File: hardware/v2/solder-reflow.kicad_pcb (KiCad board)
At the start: 2 copper layers, 86 x 65 mm, 91 parts, among them J1 ACCON, J10 PINOUT, J11 ST7789, J13 JTAG10, J2 OLED 0.91, J3 PTC_Con, J4 12V, J5 SSROUT2, J6 USB_B, J7 PINOUT, J8 PINOUT, J9 12VIN, K1 G3MB202PDC12, Q1 SS8550, Q2 SS8550, Q3 SS8050, Q4 SS8050, SW2 RST, SW3 IO0, SW4 D, SW5 U, SW6 L, SW7 R, U1 TL431LP, U2 TL074, U3 AMS1117-3.3, U4 L7805, U6 ESP32-WROOM-32D, U7 CH340C

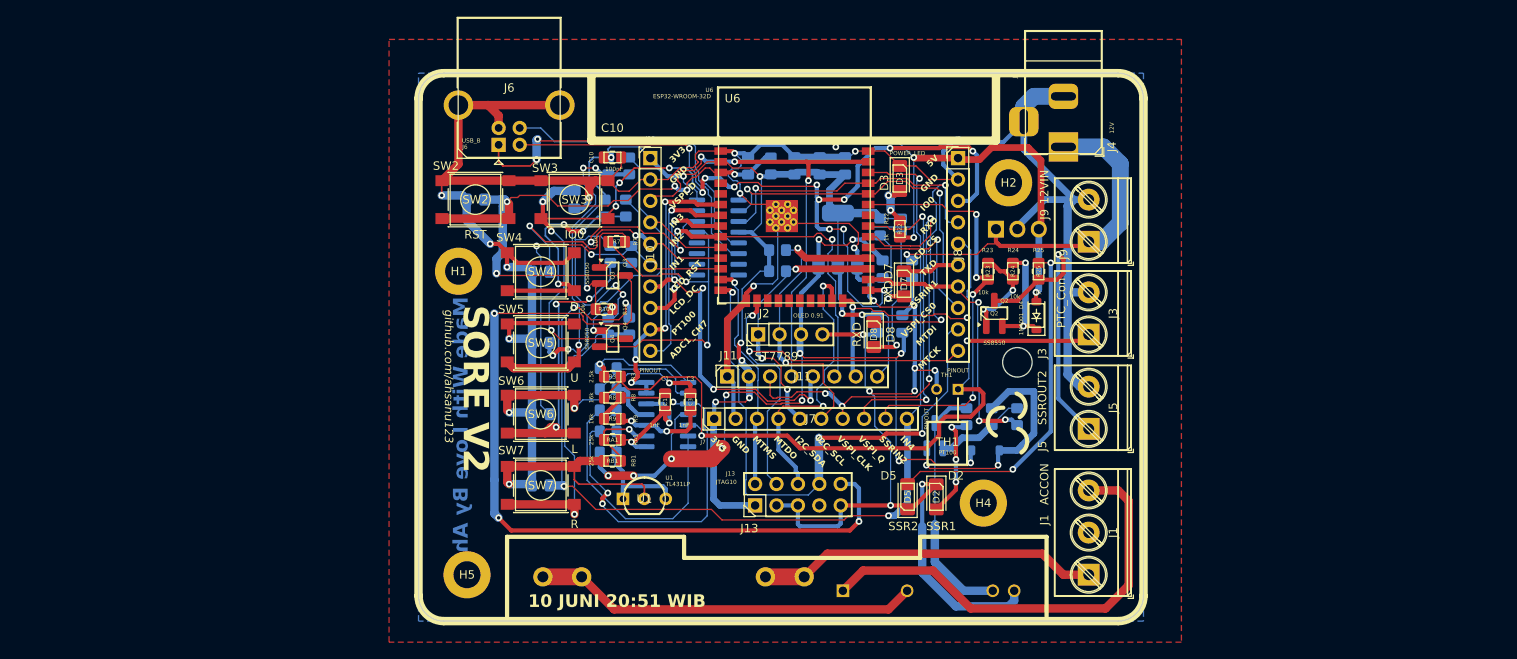
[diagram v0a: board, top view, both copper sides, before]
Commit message: feat: basic board layout finished
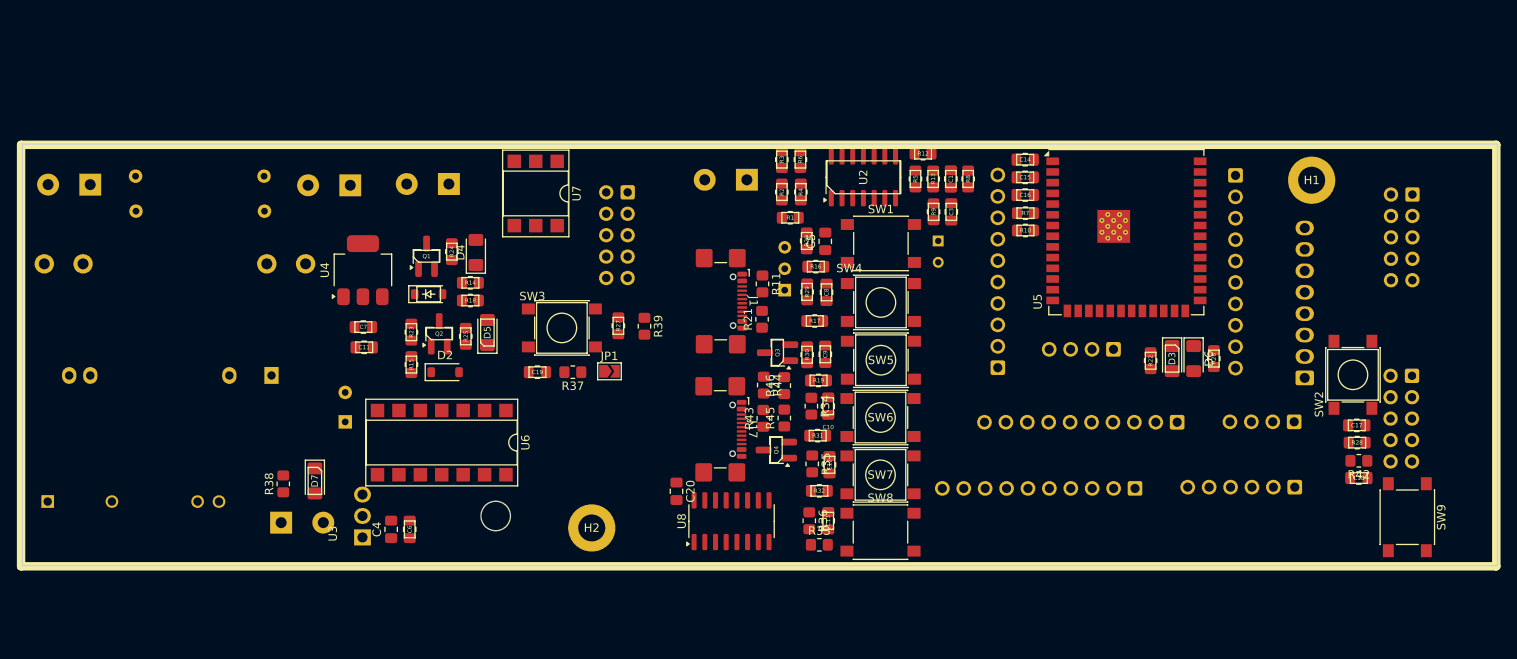
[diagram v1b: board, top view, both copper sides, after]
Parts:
- removed D8: RXD, LED_SMD:LED_1206_3216Metric_Pad1.42x1.75mm_HandSolder
- removed H4, H5: MountingHole_Pad, MountingHole:MountingHole_3.2mm_M3_DIN965_Pad
- removed J13: JTAG10, Connector_PinHeader_2.54mm:PinHeader_2x05_P2.54mm_Vertical
- removed RA1, RB1: 25k, Resistor_SMD:R_0805_2012Metric_Pad1.20x1.40mm_HandSolder
- added C20: 100nF, Capacitor_SMD:C_0805_2012Metric_Pad1.18x1.45mm_HandSolder, F.Cu at (133.1, 115.6)
- added C4: 0.33uF, Capacitor_SMD:C_0805_2012Metric_Pad1.18x1.45mm_HandSolder, F.Cu at (99.3, 120.1)
- added C5: 1uF, Capacitor_SMD:C_0805_2012Metric_Pad1.18x1.45mm_HandSolder, F.Cu at (150.7, 85.9)
- added D6: RXD, LED_SMD:LED_1206_3216Metric_Pad1.42x1.75mm_HandSolder, F.Cu at (194.4, 99.9)
- added J12: JTAG10, Connector_IDC:IDC-Header_2x05_P2.54mm_Vertical, B.Cu at (220.3, 101.9)
- added J14: SSROUT2, TerminalBlock_Phoenix:TerminalBlock_Phoenix_PT-1,5-2-5.0-H_1x02_P5.00mm_Horizontal, B.Cu at (106.1, 79.2)
- added J15: LCD_CONN, Connector_Molex:Molex_SL_171971-0010_1x10_P2.54mm_Vertical, B.Cu at (187.5, 115.3)
- added J16: UART, Connector_Molex:Molex_SL_171971-0004_1x04_P2.54mm_Vertical, B.Cu at (206.4, 107.4)
- added J17: USB_C_Receptacle_USB2.0_14P, Connector_USB:USB_C_Receptacle_GCT_USB4110, F.Cu at (137.2, 108.2)
- added J18: High_To_Low_Link, Connector_IDC:IDC-Header_2x05_P2.54mm_Vertical, B.Cu at (127.3, 80.1)
- added J19: High_To_Low_Link, Connector_IDC:IDC-Header_2x05_P2.54mm_Vertical, B.Cu at (220.4, 80.4)
- added JP1: InH11AA1, Jumper:SolderJumper-2_P1.3mm_Open_TrianglePad1.0x1.5mm, F.Cu at (125.2, 101.4)
- added PS1: HLK-2M12 12V 2W, Converter_ACDC:Converter_ACDC_Hi-Link_HLK-2Mxx, B.Cu at (85.1, 101.9)
- added R11: 5K1, Resistor_SMD:R_0805_2012Metric_Pad1.20x1.40mm_HandSolder, F.Cu at (143.3, 91.0)
- added R21: 5K1, Resistor_SMD:R_0805_2012Metric_Pad1.20x1.40mm_HandSolder, F.Cu at (143.2, 95.2)
- added R33: 10k, Resistor_SMD:R_0805_2012Metric_Pad1.20x1.40mm_HandSolder, F.Cu at (150.1, 122.0)
- added R34: 22k, Resistor_SMD:R_0805_2012Metric_Pad1.20x1.40mm_HandSolder, F.Cu at (149.1, 105.5)
- added R35: 22k, Resistor_SMD:R_0805_2012Metric_Pad1.20x1.40mm_HandSolder, F.Cu at (149.2, 112.3)
- added R36: 22k, Resistor_SMD:R_0805_2012Metric_Pad1.20x1.40mm_HandSolder, F.Cu at (148.9, 119.1)
- added R37: 22k, Resistor_SMD:R_0805_2012Metric_Pad1.20x1.40mm_HandSolder, F.Cu at (120.8, 101.5)
- added R38: 1k, Resistor_SMD:R_0805_2012Metric_Pad1.20x1.40mm_HandSolder, F.Cu at (86.5, 114.7)
- added R39: 10k, Resistor_SMD:R_0805_2012Metric_Pad1.20x1.40mm_HandSolder, F.Cu at (129.3, 96.0)
- added R40: 10k 1W, Resistor_THT:R_Axial_DIN0309_L9.0mm_D3.2mm_P15.24mm_Horizontal, B.Cu at (69.0, 82.4)
- added R41: 10k 1W, Resistor_THT:R_Axial_DIN0309_L9.0mm_D3.2mm_P15.24mm_Horizontal, B.Cu at (68.9, 78.2)
- added R42: 1k, Resistor_SMD:R_0805_2012Metric_Pad1.20x1.40mm_HandSolder, F.Cu at (214.0, 112.0)
- added R43: 5K1, Resistor_SMD:R_0805_2012Metric_Pad1.20x1.40mm_HandSolder, F.Cu at (143.4, 107.0)
- added R44: 5K1, Resistor_SMD:R_0805_2012Metric_Pad1.20x1.40mm_HandSolder, F.Cu at (143.4, 103.0)
- added R45: 10k, Resistor_SMD:R_0805_2012Metric_Pad1.20x1.40mm_HandSolder, F.Cu at (145.9, 106.9)
- added R46: 10k, Resistor_SMD:R_0805_2012Metric_Pad1.20x1.40mm_HandSolder, F.Cu at (145.9, 103.1)
- added SW1: L, Button_Switch_SMD:SW_Push_1P1T_NO_6x6mm_H9.5mm, F.Cu at (157.4, 86.2)
- added SW8: R, Button_Switch_SMD:SW_Push_1P1T_NO_6x6mm_H9.5mm, F.Cu at (157.3, 120.5)
- added SW9: Boot, Button_Switch_SMD:SW_Push_1P1T_NO_6x6mm_H9.5mm, F.Cu at (219.8, 118.7)
- added U5: ESP32-S3-WROOM-1, RF_Module:ESP32-S3-WROOM-1U, F.Cu at (186.5, 84.9)
- added U8: CH340C, Package_SO:SOIC-16_3.9x9.9mm_P1.27mm, F.Cu at (139.6, 119.2)
- C1, C3: value 1nF -> 10nF
- C10: value 100nF -> 1uF
- C11, C15: value 100nF -> 22uF; moved to F.Cu
- C12: value 100nF -> 1uF; moved to F.Cu
- C13, C8, C9: value 22uF -> 1uF; moved to F.Cu
- C14, C16, C19, D1, Q1, R1, R14, R15, R16, R17, R19, R2, R26, R28, R29, R30, R4, R5, R6: moved to F.Cu
- C17, C18: value 1uF -> 100nF; moved to F.Cu
- C2: value 1uF -> 100uF/16V; footprint Capacitor_SMD:C_0805_2012Metric_Pad1.18x1.45mm_HandSolder -> Capacitor_THT:CP_Radial_D8.0mm_P3.50mm
- C6: value 0.33uF -> 0.1uF; moved to F.Cu
- C7: value 0.1uF -> 22uF; moved to F.Cu
- D2: value SSR1 -> 1N4001; footprint LED_SMD:LED_1206_3216Metric_Pad1.42x1.75mm_HandSolder -> Diode_SMD:D_SOD-123
- D3: value POWER_LED -> TXD
- D4: value 1N4001 -> SSR2; footprint Diode_SMD:D_SOD-123 -> LED_SMD:LED_1206_3216Metric_Pad1.42x1.75mm_HandSolder
- D5: value SSR2 -> SSR1
- D7: value TXD -> POWER_LED
- J1: value ACCON -> USB_C_Receptacle_USB2.0_14P; footprint TerminalBlock_Phoenix:TerminalBlock_Phoenix_PT-1,5-3-5.0-H_1x03_P5.00mm_Horizontal -> Connector_USB:USB_C_Receptacle_GCT_USB4110
- J10, J7, J8: footprint Connector_PinHeader_2.54mm:PinHeader_1x10_P2.54mm_Vertical -> Connector_Molex:Molex_SL_171971-0010_1x10_P2.54mm_Vertical; moved to B.Cu
- J11: value ST7789 -> I2C; footprint Connector_PinSocket_2.54mm:PinSocket_1x08_P2.54mm_Vertical -> Connector_Molex:Molex_SL_171971-0004_1x04_P2.54mm_Vertical; moved to B.Cu
- J2: value OLED 0.91 -> I2S; footprint Connector_PinHeader_2.54mm:PinHeader_1x04_P2.54mm_Vertical -> Connector_Molex:Molex_SL_171971-0006_1x06_P2.54mm_Vertical; moved to B.Cu
- J3, J9, TH1, U1: moved to B.Cu
- J4: value 12V -> 220V; footprint Connector_BarrelJack:BarrelJack_Horizontal -> TerminalBlock_Phoenix:TerminalBlock_Phoenix_PT-1,5-2-5.0-H_1x02_P5.00mm_Horizontal; moved to B.Cu
- J5: value SSROUT2 -> HEATER; moved to B.Cu
- J6: value USB_B -> InputButton; footprint Connector_USB:USB_B_OST_USB-B1HSxx_Horizontal -> Connector_Molex:Molex_KK-254_AE-6410-08A_1x08_P2.54mm_Vertical; moved to B.Cu
- R10, R7: value 10k -> 4K7
- R12: value 4K7 -> 9K1; moved to F.Cu
- R13: value 4K7 -> 1K; moved to F.Cu
- R18, R27: value 1k -> 10k; moved to F.Cu
- R20: value 10k -> 22k; moved to F.Cu
- R24: value 10k -> 1k
- R31, R32: value 22k -> 10k; moved to F.Cu
- SW3: value IO0 -> SWH11AA1
- SW6: value L -> R
- U2: value TL074 -> LM324; moved to F.Cu
- U3: value AMS1117-3.3 -> L7805; footprint Package_TO_SOT_SMD:SOT-223-3_TabPin2 -> Package_TO_SOT_THT:TO-220F-3_Horizontal_TabDown
- U4: value L7805 -> AMS1117-3.3; footprint Package_TO_SOT_THT:TO-220F-3_Horizontal_TabDown -> Package_TO_SOT_SMD:SOT-223-3_TabPin2; moved to F.Cu
- U6: value ESP32-WROOM-32D -> 74LS14; footprint RF_Module:ESP32-WROOM-32D -> Package_DIP:DIP-14_W7.62mm_SMDSocket_SmallPads
- U7: value CH340C -> H11AA1; footprint Package_SO:SOIC-16_3.9x9.9mm_P1.27mm -> Package_DIP:DIP-6_W7.62mm_SMDSocket_SmallPads; moved to F.Cu
- moved J4 115.5 mm to (63.6, 79.2), turned to 180 degrees
- moved SW2 106.2 mm to (213.3, 101.8), turned to 90 degrees
- moved H1 101.8 mm to (208.4, 78.7)
- moved J9 101.4 mm to (86.2, 119.3), turned to 0 degrees
- moved J6 99.5 mm to (207.6, 102.2)
- moved C18 97.3 mm to (214.0, 114.0), turned to 0 degrees
- moved C17 97.3 mm to (213.8, 107.8)
- moved K1 94.9 mm to (68.7, 115.4)
- moved J5 92.2 mm to (94.4, 79.3), turned to 180 degrees
- moved R28 76.9 mm to (213.8, 109.8), turned to 0 degrees
- moved U4 75.3 mm to (95.9, 89.4), turned to 90 degrees
- moved D7 73.7 mm to (90.2, 114.4)
- moved R15 72.1 mm to (101.7, 100.6), turned to -90 degrees
- moved F1 69.8 mm to (89.1, 88.6)
- moved R23 68.8 mm to (101.7, 96.7), turned to -90 degrees
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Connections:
- C1 pad 1: Net-(U2D-+) -> Net-(U2C--)
- C10 pad 1: +3.3V -> /IN4
- C11 pad 1: /EN -> +3.3V
- C12 pad 1: +3.3V -> /IN5
- C13 pad 1: +3.3V -> /IN6
- C14 pad 1: /EN -> +3.3V
- C15 pad 1: /IO0 -> +3.3V
- C16 pad 1: /IN2 -> +3.3V
- C17 pad 1: /IN3 -> /EN
- C18 pad 1: /IN1 -> /IO0
- C19 pad 1: /IN4 -> Net-(JP1-A)
- C2 pad 1: +3.3V -> +12V
- C6 pad 1: +12V -> +5V
- C8 pad 1: +5V -> /IN2
- C9 pad 1: +3.3V -> /IN3
- D2 pad 1: GND -> Net-(D2-K)
- D2 pad 2: Net-(D2-A) -> +5V
- D3 pad 1: GND -> /TXD0
- D4 pad 1: Net-(D4-K) -> GND
- D4 pad 2: +5V -> Net-(D4-A)
- D7 pad 1: /TXD -> GND
- F1 pad 1: AC -> LINE
- F1 pad 2: Net-(K1-L2) -> Net-(J4-Pin_1)
- J10 pad 1: +3.3V -> /SSRIN1
- J10 pad 10: /ADC1_CH7 -> /CS0
- J10 pad 2: GND -> /SSRIN2
- J10 pad 3: /VSPI_D -> /ZC_INPUT
- J10 pad 4: /IN3 -> /PT100
- J10 pad 5: /IN2 -> /IO5
- J10 pad 6: /IN1 -> /I2C_SDA
- J10 pad 7: /LCD_RST -> /I2C_SCL
- J10 pad 8: /LCD_DC -> /IO8
- J10 pad 9: /PT100 -> /QUADHD
- J11 pad 1: GND -> +3.3V
- J11 pad 2: +3.3V -> /I2C_SDA
- J11 pad 3: /VSPI_CLK -> /I2C_SCL
- J11 pad 4: /VSPI_D -> GND
- J2 pad 1: /I2C_SDA -> +3.3V
- J2 pad 2: /I2C_SCL -> /MCLK
- J2 pad 3: +5V -> /BCLK
- J2 pad 4: GND -> /WS
- J4 pad 1: +12V -> Net-(J4-Pin_1)
- J4 pad 2: GND -> NEUT
- J5 pad 1: Net-(J5-Pin_1) -> LINE
- J5 pad 2: GND -> Net-(J5-Pin_2)
- J6 pad 1: +5V -> /sw1
- J6 pad 2: Net-(J6-D-) -> /sw2
- J6 pad 3: Net-(J6-D+) -> /sw3
- J6 pad 4: GND -> /sw4
- J6 pad 5: GND -> /sw5
- J7 pad 1: +3.3V -> /MOSI
- J7 pad 10: /IN4 -> /IN5
- J7 pad 2: GND -> /SCLK
- J7 pad 3: /MTMS -> /MISO
- J7 pad 4: /MTDO -> /QUADWP
- J7 pad 5: /I2C_SDA -> /IN1
- J7 pad 6: /I2C_SCL -> /IN2
- J7 pad 7: /VSPI_CLK -> /TXD0
- J7 pad 8: /VSPI_Q -> /RXD0
- J7 pad 9: /SSRIN2 -> /IN4
- J8 pad 1: +5V -> /IN6
- J8 pad 10: /MTCK -> /DIO
- J8 pad 2: GND -> /MCLK
- J8 pad 3: /IO0 -> /MTCK
- J8 pad 4: /RXD -> /MTDO
- J8 pad 5: /LCD_CS -> /MTDI
- J8 pad 6: /TXD -> /MTMS
- J8 pad 7: /SSRIN1 -> /BCLK
- J8 pad 8: /VSPI_CS0 -> /IN3
- J8 pad 9: /MTDI -> /WS
- K1 pad 1: Net-(J1-Pin_3) -> Net-(J5-Pin_2)
- K1 pad 2: Net-(K1-L2) -> NEUT
- Q1 pad 3: Net-(K1-+) -> Net-(J14-Pin_1)
- Q2 pad 2: Net-(D4-K) -> Net-(D2-K)
- Q2 pad 3: Net-(J5-Pin_1) -> Net-(K1-+)
- R10 pad 1: Net-(Q4-B) -> /I2C_SCL
- R10 pad 2: /RTS -> +3.3V
- R12 pad 1: /I2C_SDA -> /PT100
- R12 pad 2: +3.3V -> Net-(U2D--)
- R13 pad 1: /I2C_SCL -> Net-(U2D--)
- R13 pad 2: +3.3V -> GND
- R15 pad 1: /SSRIN1 -> Net-(Q2-B)
- R15 pad 2: Net-(Q1-B) -> Net-(D2-K)
- R16 pad 2: Net-(R16-Pad2) -> /sw1
- R17 pad 2: Net-(R17-Pad2) -> /sw2
- R18 pad 1: Net-(D2-A) -> /SSRIN2
- R18 pad 2: Net-(K1-+) -> Net-(Q1-B)
- R19 pad 2: Net-(R19-Pad2) -> /sw3
- R20 pad 1: +3.3V -> /IN1
- R20 pad 2: Net-(R20-Pad2) -> /sw1
- R22 pad 1: Net-(D3-A) -> +3.3V
- R22 pad 2: +5V -> Net-(D3-A)
- R23 pad 1: /SSRIN2 -> /SSRIN1
- R24 pad 1: Net-(Q2-B) -> Net-(D4-A)
- R24 pad 2: Net-(D4-K) -> Net-(J14-Pin_1)
- R25 pad 2: Net-(J5-Pin_1) -> Net-(K1-+)
- R26 pad 2: Net-(D7-A) -> Net-(D6-A)
- R27 pad 2: Net-(D8-A) -> Net-(R27-Pad2)
- R29 pad 1: /IN1 -> /IN2
- R29 pad 2: Net-(R16-Pad2) -> /sw2
- R30 pad 1: /IN2 -> /IN3
- R30 pad 2: Net-(R17-Pad2) -> /sw3
- R31 pad 1: /IN3 -> +3.3V
- R31 pad 2: Net-(R19-Pad2) -> /sw4
- R32 pad 1: /IN4 -> +3.3V
- R32 pad 2: Net-(R20-Pad2) -> /sw5
- R7 pad 1: Net-(Q3-B) -> /I2C_SDA
- R7 pad 2: /DTR -> +3.3V
- SW3 pad 2: /IO0 -> Net-(R27-Pad2)
- SW4 pad 2: Net-(R17-Pad2) -> /sw2
- SW5 pad 2: Net-(R19-Pad2) -> /sw3
- SW6 pad 2: Net-(R16-Pad2) -> /sw4
- SW7 pad 2: Net-(R20-Pad2) -> /sw5
- U2 pad 12: Net-(U2D-+) -> Net-(U2C--)
- U2 pad 13: /PT100 -> Net-(U2D--)
- U2 pad 8: Net-(U2D-+) -> Net-(U2C--)
- U3 pad 1: GND -> +12V
- U3 pad 2: +3.3V -> GND
- U4 pad 1: +12V -> GND
- U4 pad 2: GND -> +3.3V
- U6 pad 1: GND -> Net-(R39-Pad2)
- U6 pad 10: /IN3 -> (no net)
- U6 pad 11: /IN2 -> (no net)
- U6 pad 12: /IN1 -> (no net)
- U6 pad 13: /MTMS -> (no net)
- U6 pad 14: /MTDI -> +5V
- U6 pad 2: +3.3V -> /ZC_INPUT
- U6 pad 3: /EN -> (no net)
- U6 pad 4: unconnected-(U6-SENSOR_VP-Pad4) -> (no net)
- U6 pad 5: unconnected-(U6-SENSOR_VN-Pad5) -> (no net)
- U6 pad 6: /PT100 -> (no net)
- U6 pad 7: /ADC1_CH7 -> GND
- U6 pad 8: /LCD_RST -> (no net)
- U6 pad 9: /LCD_DC -> (no net)
- U7 pad 1: GND -> Net-(R40-Pad2)
- U7 pad 2: /TXD -> Net-(R41-Pad2)
- U7 pad 3: /RXD -> unconnected-(U7-NC-Pad3)
- U7 pad 4: +3.3V -> GND
- U7 pad 5: Net-(J6-D+) -> Net-(R39-Pad2)
- U7 pad 6: Net-(J6-D-) -> Net-(JP1-B)
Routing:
- net GND: track 482.1 -> 0.00 mm, vias 23 -> 0
- net +5V: track 222.0 -> 0.00 mm, vias 18 -> 0
- net /EN: track 173.1 -> 0.00 mm, vias 8 -> 0
- net +3.3V: track 169.2 -> 0.00 mm, vias 11 -> 0
- net /IO0: track 126.8 -> 0.00 mm, vias 17 -> 0
- net /IN4: track 123.0 -> 0.00 mm, vias 5 -> 0
- net /PT100Voltage: track 86.2 -> 0.00 mm, vias 2 -> 0
- net /VSPI_D: track 72.5 -> 0.00 mm, vias 3 -> 0
- net /MTDI: track 68.0 -> 0.00 mm, vias 3 -> 0
- net /RXD: track 60.8 -> 0.00 mm, vias 3 -> 0
- net /VSPI_CLK: track 55.2 -> 0.00 mm, vias 4 -> 0
- net Net-(J1-Pin_3): track 53.2 -> 0.00 mm
- net /MTCK: track 52.0 -> 0.00 mm, vias 2 -> 0
- net /SSRIN2: track 49.1 -> 0.00 mm, vias 4 -> 0
- net /LCD_RST: track 48.8 -> 0.00 mm, vias 5 -> 0
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- removed copper zone on F.Cu, net (none)
- removed copper zone on B.Cu, net GND
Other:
- board size 86 x 65 mm -> 175 x 50 mm
- board text added: "HIGH"
- board text added: "LOW"
- board text removed: "10 JUNI 20:51 WIB"
- board text removed: "3V3"
- board text removed: "5V"
- board text removed: "ADC1_CH7"
- board text removed: "GND"
- board text removed: "I2C_SCL"
- board text removed: "I2C_SDA"
- board text removed: "IN1"
- board text removed: "IN2"
- board text removed: "IN3"
- board text removed: "IN4"
- board text removed: "IO0"
- board text removed: "LCD_CS"
- board text removed: "LCD_DC"
- board text removed: "LCD_RST"
- board text removed: "MTCK"
- board text removed: "MTDI"
- board text removed: "MTDO"
- board text removed: "MTMS"
- board text removed: "Made With Love By Ah"
- board text removed: "PT100"
- board text removed: "RXD"
- board text removed: "SORE Solder Reflow"
- board text removed: "SORE V2"
- board text removed: "SSRIN1"
- board text removed: "SSRIN2"
- board text removed: "TXD"
- board text removed: "VSPI_CLK"
- board text removed: "VSPI_CS0"
- board text removed: "VSPI_D"
- board text removed: "VSPI_Q"
- board text removed: "github.com/ahsanu123"

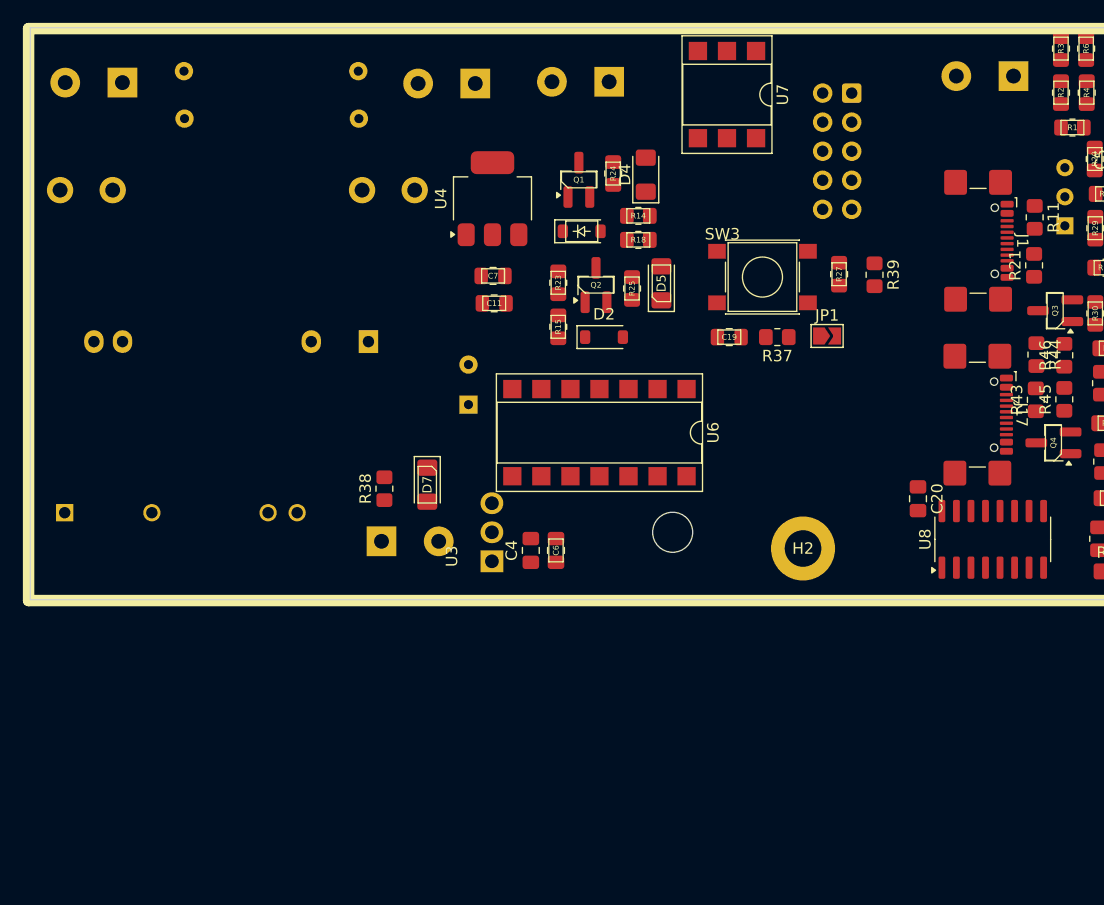
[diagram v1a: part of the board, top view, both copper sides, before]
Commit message: feat: routing part 1
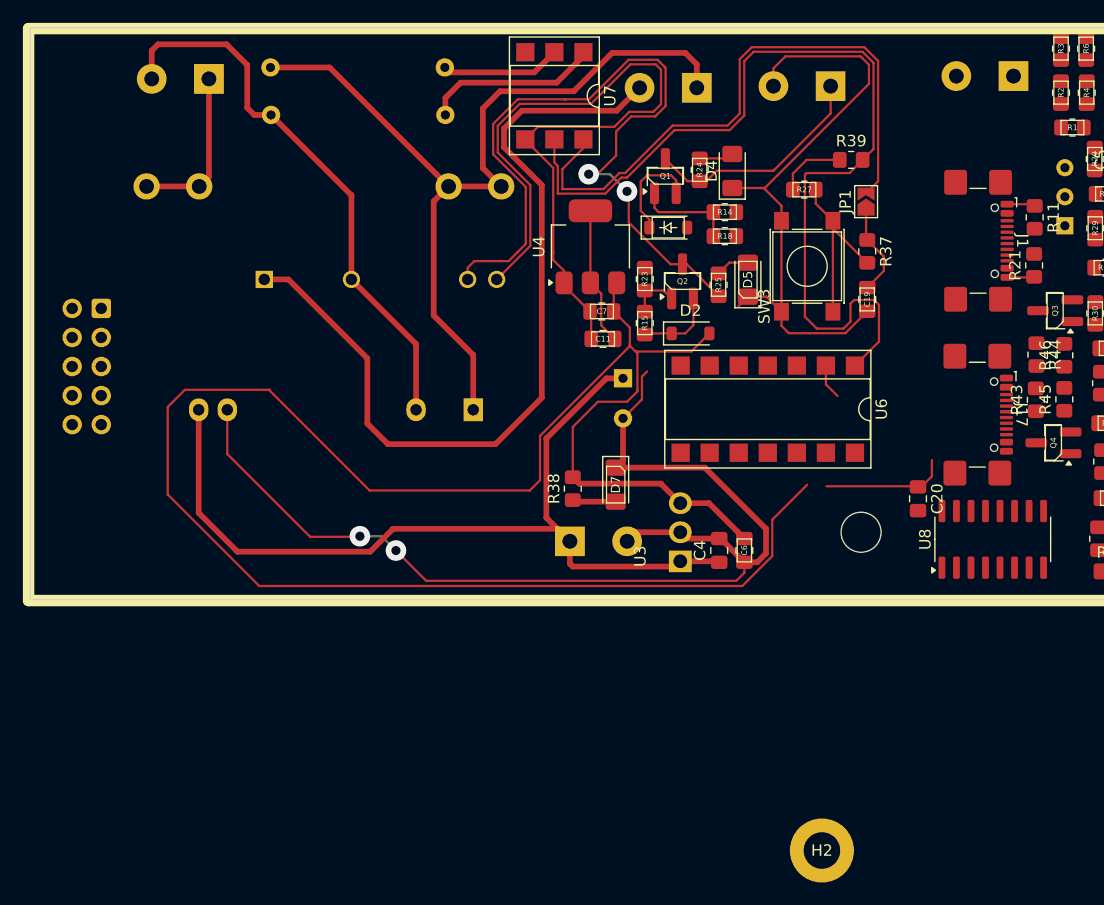
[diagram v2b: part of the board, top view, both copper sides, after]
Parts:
- moved J18 68.3 mm to (61.7, 99.0)
- moved K1 26.8 mm to (86.1, 95.0)
- moved H2 26.5 mm to (124.7, 146.3)
- moved J14 19.4 mm to (125.5, 79.5)
- moved J5 19.4 mm to (113.8, 79.7)
- moved U3 16.5 mm to (112.3, 121.1)
- moved C4 16.5 mm to (115.7, 120.1)
- moved C6 16.5 mm to (117.9, 120.1)
- moved D7 16.5 mm to (106.7, 114.4)
- moved J9 16.5 mm to (102.7, 119.3)
- moved R38 16.5 mm to (102.9, 114.7)
- moved U7 15.1 mm to (101.3, 80.4)
- moved U6 14.9 mm to (120.0, 107.8)
- moved C2 13.7 mm to (107.3, 105.1), turned to -90 degrees
- moved C19 12.5 mm to (128.7, 98.2), turned to -90 degrees
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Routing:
- net GND: track 0.00 -> 223.4 mm, vias 0 -> 2
- net +5V: track 0.00 -> 171.4 mm
- net Net-(R39-Pad2): track 0.00 -> 82.9 mm
- net +12V: track 0.00 -> 78.2 mm
- net LINE: track 0.00 -> 76.6 mm
- net Net-(J5-Pin_2): track 0.00 -> 73.5 mm
- net Net-(K1-+): track 0.00 -> 67.7 mm, vias 0 -> 2
- net Net-(JP1-B): track 0.00 -> 53.1 mm
- net NEUT: track 0.00 -> 48.9 mm
- net +3.3V: track 0.00 -> 29.1 mm
- net Net-(J14-Pin_1): track 0.00 -> 20.1 mm
- net Net-(R27-Pad2): track 0.00 -> 16.2 mm
- net Net-(R40-Pad2): track 0.00 -> 15.4 mm
- net Net-(J4-Pin_1): track 0.00 -> 14.4 mm
- net Net-(R41-Pad2): track 0.00 -> 10.5 mm
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
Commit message: feat: routing part 2
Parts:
- moved R22 29.6 mm to (206.7, 76.2), turned to 0 degrees
- moved J6 29.2 mm to (178.4, 100.2), turned to -90 degrees
- moved D3 25.8 mm to (206.1, 78.4), turned to 0 degrees
- moved R42 22.9 mm to (205.8, 90.5), turned to 0 degrees
- moved C18 22.9 mm to (205.8, 92.6), turned to 180 degrees
- moved R28 22.8 mm to (205.8, 88.5)
- moved C17 22.8 mm to (205.8, 86.5)
- moved J10 22.8 mm to (169.8, 78.2), turned to -90 degrees
- moved SW9 22.5 mm to (212.3, 97.5)
- moved D6 22.1 mm to (206.1, 81.0), turned to 0 degrees
- moved R26 19.3 mm to (206.7, 83.2), turned to 0 degrees
- moved J11 17.3 mm to (169.8, 107.2), turned to -90 degrees
- moved J7 15.2 mm to (186.6, 121.3), turned to 90 degrees
- moved SW2 15.0 mm to (212.2, 86.9), turned to -90 degrees
- moved R4 14.1 mm to (159.7, 87.8), turned to 0 degrees
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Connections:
- J10 pad 1: /SSRIN1 -> /PT100
- J10 pad 10: /CS0 -> /USB_D-
- J10 pad 2: /SSRIN2 -> /IO5
- J10 pad 3: /ZC_INPUT -> /I2C_SDA
- J10 pad 4: /PT100 -> /I2C_SCL
- J10 pad 5: /IO5 -> /IN1
- J10 pad 6: /I2C_SDA -> /IN2
- J10 pad 7: /I2C_SCL -> /IN4
- J10 pad 8: /IO8 -> /IN5
- J10 pad 9: /QUADHD -> /IO8
- J7 pad 1: /MOSI -> /USB_D+
- J7 pad 10: /IN5 -> /IN6
- J7 pad 2: /SCLK -> /ZC_INPUT
- J7 pad 3: /MISO -> /IN3
- J7 pad 4: /QUADWP -> /QUADHD
- J7 pad 5: /IN1 -> /CS0
- J7 pad 6: /IN2 -> /MOSI
- J7 pad 7: /TXD0 -> /SCLK
- J7 pad 8: /RXD0 -> /MISO
- J7 pad 9: /IN4 -> /QUADWP
- J8 pad 1: /IN6 -> /TXD0
- J8 pad 10: /DIO -> /WS
- J8 pad 2: /MCLK -> /RXD0
- J8 pad 3: /MTCK -> /MTMS
- J8 pad 4: /MTDO -> /MTDI
- J8 pad 5: /MTDI -> /MTDO
- J8 pad 6: /MTMS -> /MTCK
- J8 pad 7: /BCLK -> /MCLK
- J8 pad 8: /IN3 -> /BCLK
- J8 pad 9: /WS -> /DIO
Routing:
- net GND: track 223.4 -> 467.1 mm
- net +3.3V: track 29.1 -> 86.1 mm
- net /sw6: track 0.00 -> 41.4 mm
- net /PT100: track 0.00 -> 38.9 mm
- net /USB_D+: track 0.00 -> 37.5 mm
- net +5V: track 171.4 -> 208.1 mm
- net /ZC_INPUT: track 3.08 -> 33.6 mm
- net /IN3: track 0.00 -> 29.6 mm
- net /IO0: track 0.00 -> 26.8 mm
- net /QUADHD: track 0.00 -> 24.3 mm
- net /CS0: track 0.00 -> 21.7 mm
- net /PT100Voltage: track 0.00 -> 20.9 mm
- net Net-(U2A-+): track 0.00 -> 20.5 mm
- net /MOSI: track 0.00 -> 19.0 mm
- net /USB_D-: track 0.00 -> 17.4 mm
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
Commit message: feat: attempt to finish routing
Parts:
- removed J10: PINOUT, Connector_Molex:Molex_SL_171971-0010_1x10_P2.54mm_Vertical
- removed J12: JTAG10, Connector_IDC:IDC-Header_2x05_P2.54mm_Vertical
- removed J18, J19: High_To_Low_Link, Connector_IDC:IDC-Header_2x05_P2.54mm_Vertical
- removed R12: 9K1, Resistor_SMD:R_0805_2012Metric_Pad1.20x1.40mm_HandSolder
- removed R13: 1K, Resistor_SMD:R_0805_2012Metric_Pad1.20x1.40mm_HandSolder
- removed R2, R4, R5, R6: 25k, Resistor_SMD:R_0805_2012Metric_Pad1.20x1.40mm_HandSolder
- removed R3: 2.5k, Resistor_SMD:R_0805_2012Metric_Pad1.20x1.40mm_HandSolder
- removed R8, R9: 16k, Resistor_SMD:R_0805_2012Metric_Pad1.20x1.40mm_HandSolder
- removed TH1: PT100, Package_TO_SOT_THT:TO-92-2_Horizontal2
- removed U1: TL431LP, Package_TO_SOT_THT:TO-92_Inline_Wide
- removed U2: LM324, Package_SO:SOIC-14_3.9x8.7mm_P1.27mm
- added C21: 100nF, Capacitor_SMD:C_0805_2012Metric_Pad1.18x1.45mm_HandSolder, F.Cu at (173.3, 99.8)
- added J13: RTD_PT100, TerminalBlock_Phoenix:TerminalBlock_Phoenix_PT-1,5-3-5.0-H_1x03_P5.00mm_Horizontal, F.Cu at (181.8, 94.3)
- added JP2: 3_OR_2_Wire, Jumper:SolderJumper-3_P1.3mm_Open_RoundedPad1.0x1.5mm, F.Cu at (158.9, 93.2)
- added JP3: 2_Wire, Jumper:SolderJumper-2_P1.3mm_Open_TrianglePad1.0x1.5mm, F.Cu at (161.5, 92.6)
- added U9: MAX31865xTP, Package_DFN_QFN:TQFN-20-1EP_5x5mm_P0.65mm_EP3.25x3.25mm, F.Cu at (171.9, 94.1)
- C1, C3: value 10nF -> 100nF
- J3: value PTC_Con -> PINOUT; footprint TerminalBlock_Phoenix:TerminalBlock_Phoenix_PT-1,5-2-5.0-H_1x02_P5.00mm_Horizontal -> Connector_Molex:Molex_SL_171971-0010_1x10_P2.54mm_Vertical
- R1: value 25k -> 400 1%
- moved SW2 100.0 mm to (112.5, 93.3)
- moved R28 95.6 mm to (111.1, 101.5), turned to 180 degrees
- moved C17 95.6 mm to (111.1, 99.4), turned to 0 degrees
- moved SW9 93.3 mm to (119.1, 93.3)
- moved R42 91.6 mm to (114.9, 101.5)
- moved C18 91.1 mm to (115.0, 99.4)
- moved R10 82.5 mm to (113.5, 141.4)
- moved R7 82.5 mm to (113.5, 139.4)
- moved SW8 80.5 mm to (91.0, 138.3), turned to 180 degrees
- moved J16 78.9 mm to (141.2, 75.5), turned to 0 degrees
- moved U3 78.7 mm to (133.1, 45.1), turned to 0 degrees
- moved J6 76.2 mm to (102.3, 103.1)
- moved J8 75.6 mm to (126.0, 91.2), turned to 0 degrees
- moved J2 75.0 mm to (136.2, 83.4), turned to 0 degrees
- moved C4 73.9 mm to (134.0, 48.5), turned to 0 degrees
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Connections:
- C3 pad 1: Net-(U2C-+) -> +3.3V
- J3 pad 1: /PT100Voltage -> /PT100
- J3 pad 2: GND -> /IO5
- J7 pad 1: /USB_D+ -> /IN6
- J7 pad 10: /IN6 -> /USB_D+
- J7 pad 2: /ZC_INPUT -> /QUADWP
- J7 pad 3: /IN3 -> /MISO
- J7 pad 4: /QUADHD -> /SCLK
- J7 pad 5: /CS0 -> /MOSI
- J7 pad 6: /MOSI -> /CS0
- J7 pad 7: /SCLK -> /QUADHD
- J7 pad 8: /MISO -> /IN3
- J7 pad 9: /QUADWP -> /ZC_INPUT
- R1 pad 1: +2V5 -> Net-(U9-BIAS)
- R1 pad 2: +5V -> Net-(U9-ISENSOR)
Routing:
- net GND: track 467.1 -> 610.8 mm
- net +3.3V: track 86.1 -> 215.2 mm, vias 0 -> 2
- net Net-(R39-Pad2): track 82.9 -> 17.6 mm
- net Net-(J5-Pin_2): track 73.5 -> 8.97 mm
- net Net-(J13-Pin_1): track 9.07 -> 64.9 mm
- net NEUT: track 48.9 -> 104.0 mm
- net Net-(J13-Pin_2): track 3.99 -> 57.2 mm
- net Net-(K1-+): track 67.7 -> 15.5 mm, vias 2 -> 0
- net Net-(JP1-B): track 53.1 -> 4.66 mm
- net +5V: track 208.1 -> 252.9 mm, vias 0 -> 4
- net Net-(J13-Pin_3): track 0.00 -> 42.7 mm
- net LINE: track 76.6 -> 118.2 mm
- net /EN: track 15.2 -> 43.6 mm
- net /I2C_SCL: track 9.42 -> 32.6 mm
- net /PT100: track 38.9 -> 17.1 mm
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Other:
- board outline removed
- board text removed: "HIGH"
- board text removed: "LOW"
